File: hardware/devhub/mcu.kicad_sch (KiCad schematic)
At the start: 19 parts, among them J4 SWD, J9 UART debug, U3 STM32G0B1CEU6

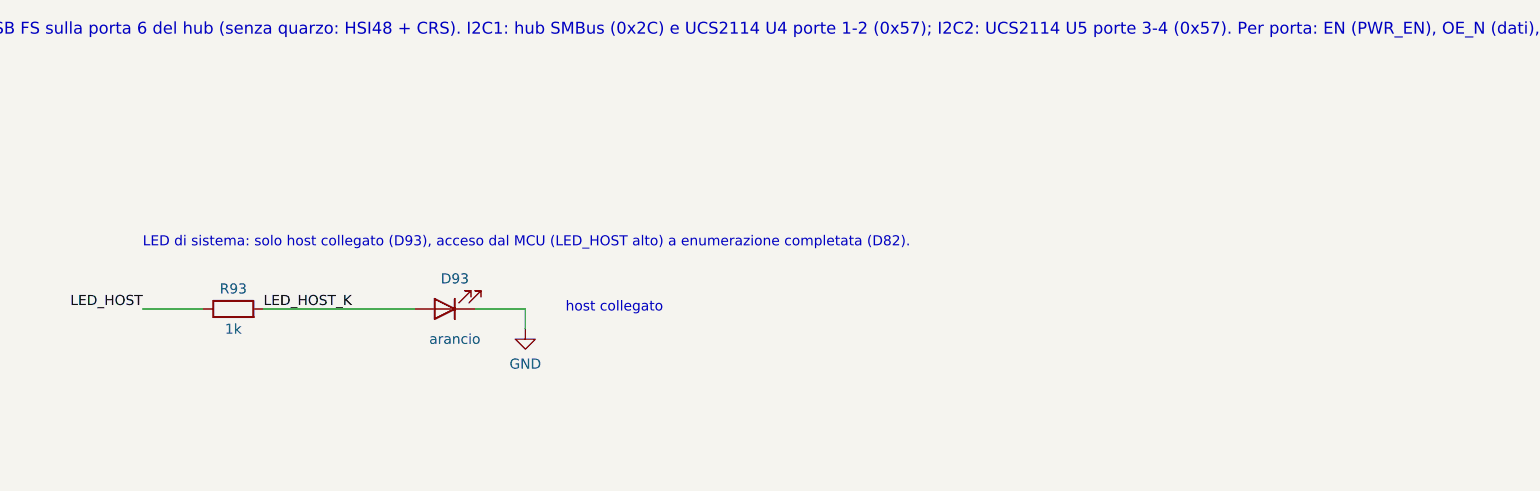
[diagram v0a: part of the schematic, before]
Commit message: Restore relay LED, larger NC/NO jumper, PCB routing progress (D89, D90)
- D90/R90 relay LED back on RLY1, in the front LED row in line with SW1;
  host LED D93/R93 moved to the rear next to J1
- JP2: project footprint with 2.0x3.0 mm pads, 2.4 mm pitch and 1.0 mm
  bridge for 3 A relay contacts
- U13: 0.2 mm tracks from pads 8/9 alongside the corner pads, no clearance
  exception
- Routing and placement progress, zone defaults, schematic layout cleanup
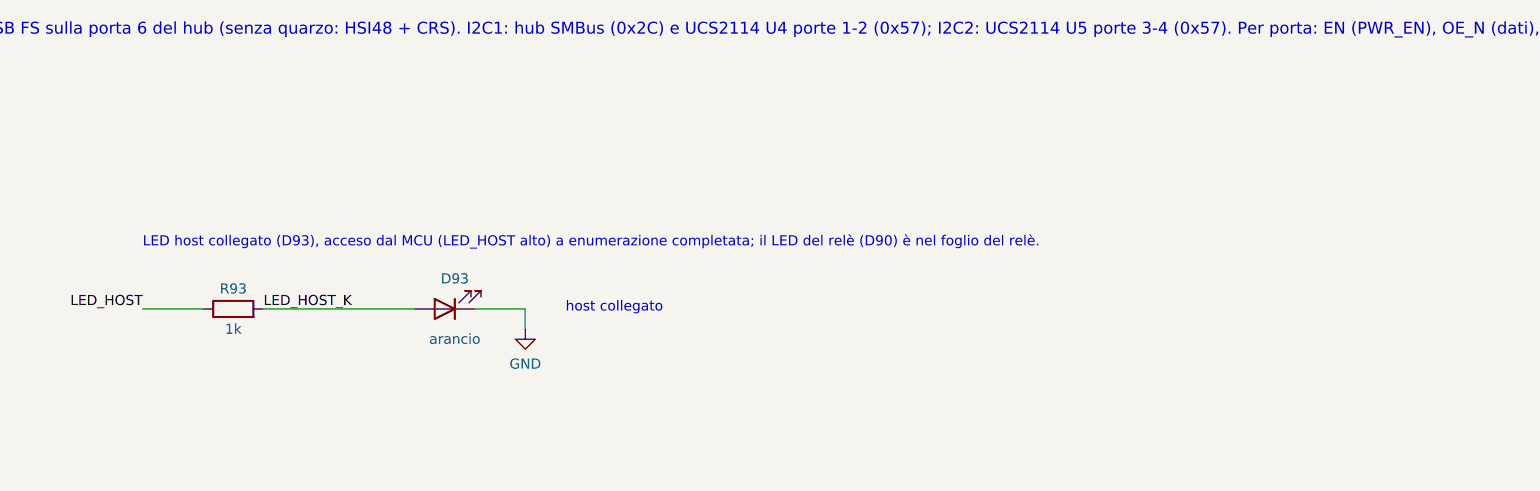
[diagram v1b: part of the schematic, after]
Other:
- note added: "LED host collegato (D93), acceso dal MCU (LED_HOST alto) a enumerazione completata; il LED del relè (D90) è nel foglio del relè."
- note removed: "LED di sistema: solo host collegato (D93), acceso dal MCU (LED_HOST alto) a enumerazione completata (D82)."

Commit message: PCB routing complete, package in values, MPN fields
- Routing finished; ESD_FANOUT rule area for D20 centre pins
- Vias keep inner-layer rings only where connected; GND reference vias
  next to SWD and I2C layer changes
- Value field of chip R/C/LED includes the package (0402...1206)
- New fields MPN lcsc, MPN mouser, MPN digikey; LCSC codes for R60/R61,
  U3, U4/U5 and supplier codes completed; JP2 marked DNP on the PCB
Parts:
- C40: value 4.7u -> 4.7u 0603; MPN digikey (none) -> CL10A475KO8NNNC; MPN lcsc (none) -> CL10A475KO8NNNC; MPN mouser (none) -> CL10A475KO8NNNC
- C41, C42, C46: value 100n -> 100n 0402; MPN digikey (none) -> CC0402KRX7R7BB104; MPN lcsc (none) -> CC0402KRX7R7BB104; MPN mouser (none) -> CC0402KRX7R7BB104
- D93: value arancio -> arancio 0805; MPN digikey (none) -> LTST-C171KFKT; MPN lcsc (none) -> LTST-C171KFKT; MPN mouser (none) -> LTST-C171KFKT
- J4: MPN digikey (none) -> FTSH-105-01-L-DV-K; MPN lcsc (none) -> FTSH-105-01-L-DV-K; MPN mouser (none) -> FTSH-105-01-L-DV-K
- J9: MPN digikey (none) -> 61300311121; MPN lcsc (none) -> 2.54-1*3P; MPN mouser (none) -> 61300311121
- R40, R41, R50, R51: value 4.7k -> 4.7k 0603; MPN digikey (none) -> RC0603FR-074K7L; MPN lcsc (none) -> RC0603FR-074K7L; MPN mouser (none) -> RC0603FR-074K7L
- R42, R43, R44, R45, R48, R49: value 10k -> 10k 0603; MPN digikey (none) -> RC0603FR-0710KL; MPN lcsc (none) -> FRC0603F1002TS; MPN mouser (none) -> RC0603FR-0710KL
- R93: value 1k -> 1k 0603; MPN digikey (none) -> RC0603FR-071KL; MPN lcsc (none) -> 0603WAF1001T5E; MPN mouser (none) -> RC0603FR-071KL
- U3: MPN digikey (none) -> STM32G0B1CEU6; MPN lcsc (none) -> STM32G0B1CEU6; MPN mouser (none) -> STM32G0B1CEU6; lcsc (none) -> C2829190; mouser (none) -> 511-STM32G0B1CEU6

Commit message: Test points, LED host moved, board finished (D92)
- 14 test points: GND loops TP1/TP10 (Keystone 5001), pads for +5V, +3V3,
  I2C1/I2C2, HUB_RST_N, EFUSE_FLT_N and VBUS_P1-P4
- D93/R93 moved to the rear, left of J1
- Button symbols: generic Value, function in Description; PCB aligned
- Docs: decision D92, components, PCB test rules, LED host position
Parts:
- added TP10: Keystone 5001, TestPoint:TestPoint_Keystone_5000-5004_Miniature, symbol Connector:TestPoint
- added TP4: I2C1_SCL, TestPoint:TestPoint_Pad_D1.5mm, symbol Connector:TestPoint
- added TP5: I2C1_SDA, TestPoint:TestPoint_Pad_D1.5mm, symbol Connector:TestPoint
- added TP6: I2C2_SCL, TestPoint:TestPoint_Pad_D1.5mm, symbol Connector:TestPoint
- added TP7: I2C2_SDA, TestPoint:TestPoint_Pad_D1.5mm, symbol Connector:TestPoint
- added TP8: HUB_RST_N, TestPoint:TestPoint_Pad_D1.5mm, symbol Connector:TestPoint
- added TP9: EFUSE_FLT_N, TestPoint:TestPoint_Pad_D1.5mm, symbol Connector:TestPoint
- J9: now left out of the parts list
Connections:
- net EFUSE_FLT_N: now also TP9.1
- net GND: now also TP10.1
- net HUB_RST_N: now also TP8.1
- net I2C1_SCL: now also TP4.1
- net I2C1_SDA: now also TP5.1
- net I2C2_SCL: now also TP6.1
- net I2C2_SDA: now also TP7.1
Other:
- note added: "Test point: bus I2C, reset del hub, FLT dell'eFuse e anello GND (D92)"
